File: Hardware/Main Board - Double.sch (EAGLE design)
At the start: 80 parts, among them J1 MICROMOD-2222-C, J10 MICRO-SD-PUSH-PUSH-EXT-PIN, J2 Vertical Qwiic Connector, J4 QWIIC_RIGHT_ANGLE, J5 CORTEX_JTAG_DEBUG_MINIMUM_PTH, J6 MICROMOD_FUNCTION_MAIN, J7 MICROMOD_FUNCTION_MAIN, Q1 3.1A/30V/105mΩ, U1 STG3856QTR, U2 MCP73831, U3 ESD Diode, U4 3.3V, U5 AP7361C-33

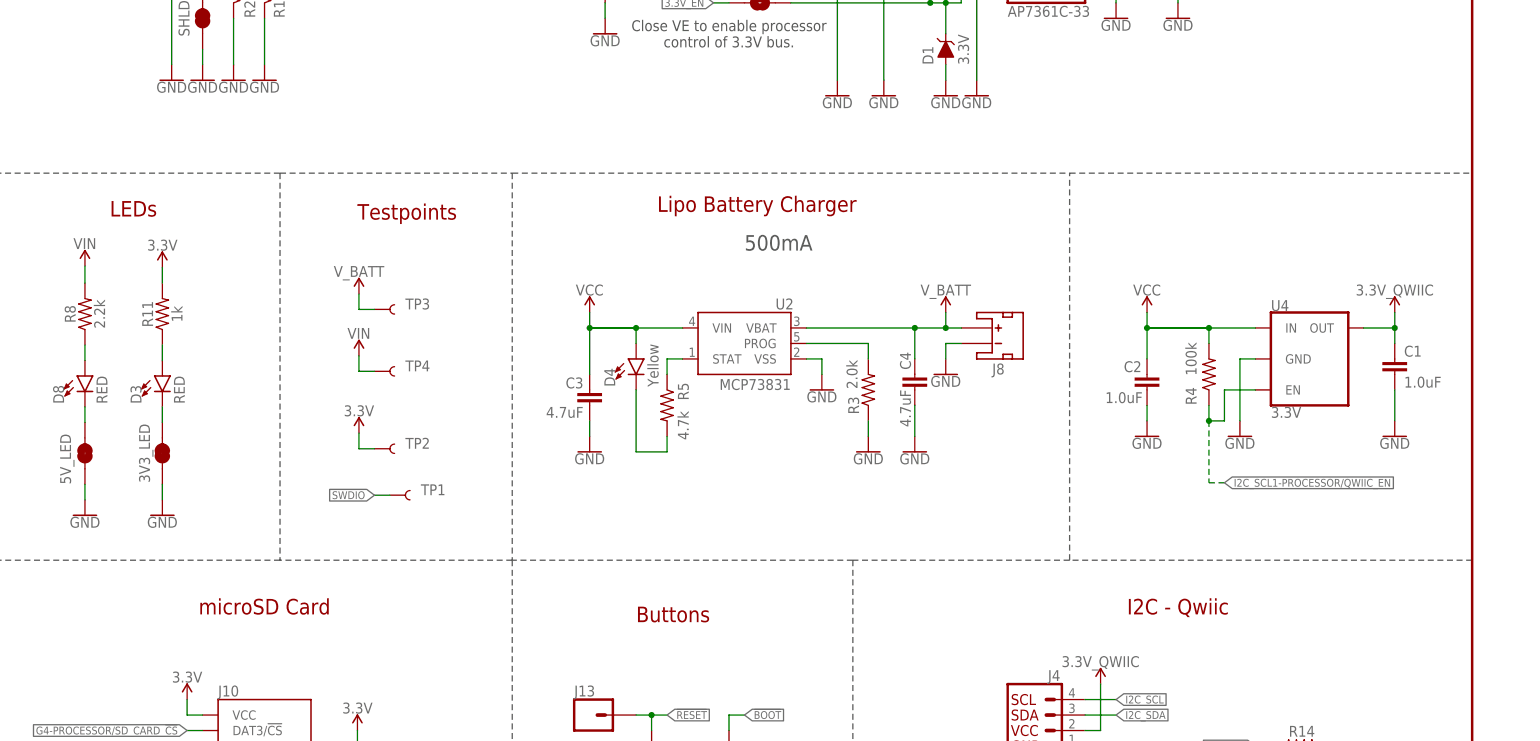
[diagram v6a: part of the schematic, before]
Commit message: Updates text in schematic
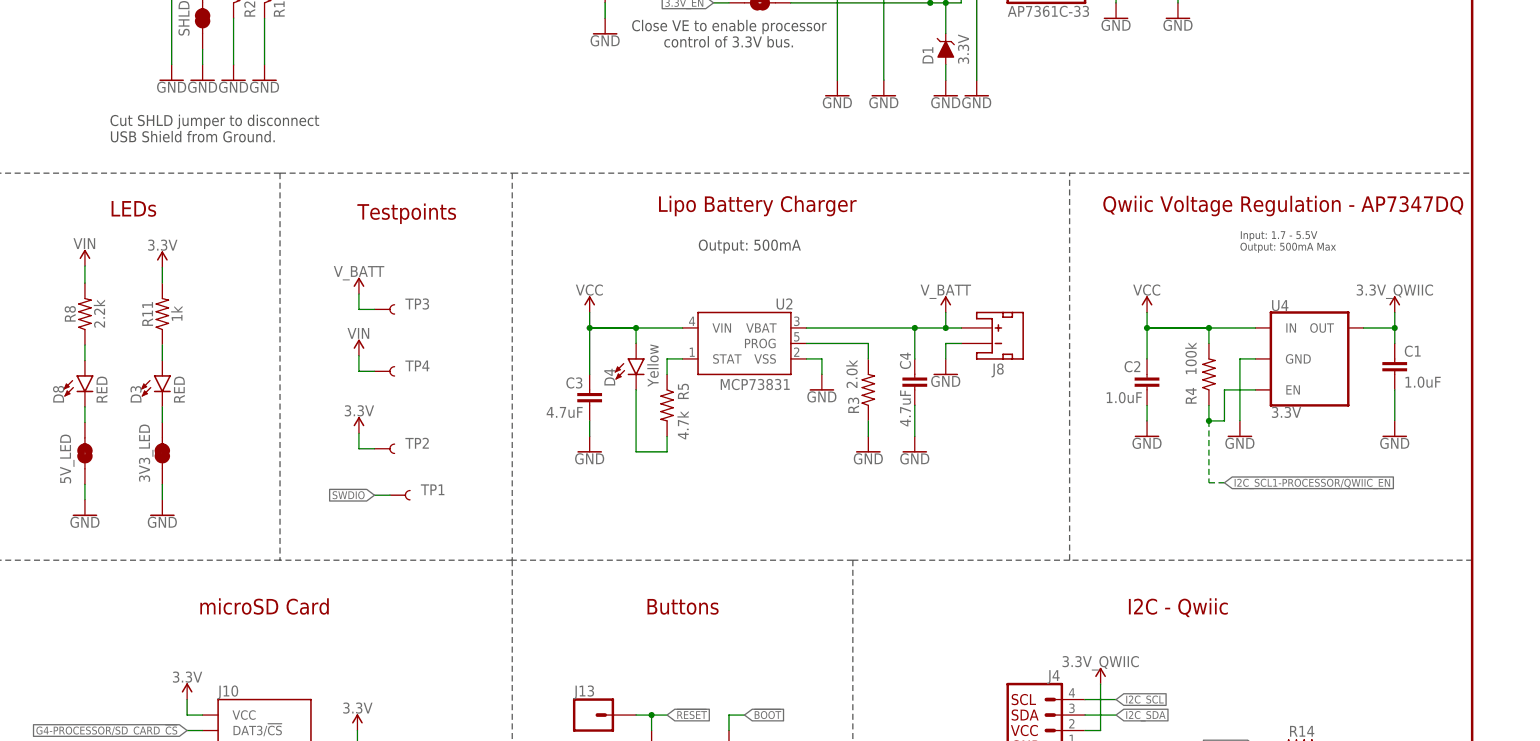
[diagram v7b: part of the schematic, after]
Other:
- note added: "Cut SHLD jumper to disconnect USB Shield from Ground."
- note added: "Input: 1.7 - 5.5V Output: 500mA Max"
- note added: "Output: 500mA"
- note added: "Qwiic Voltage Regulation - AP7347DQ"
- note removed: "500mA"
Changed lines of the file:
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@@
 <wire x1="274.32" y1="76.2" x2="330.2" y2="76.2" width="0.2032" layer="97" style="longdash"/>
 <wire x1="274.32" y1="195.58" x2="274.32" y2="132.08" width="0.2032" layer="97" style="longdash"/>
-<text x="294.64" y="121.92" size="2.54" layer="94" font="vector">Buttons</text>
+<text x="302.26" y="124.46" size="2.54" layer="94" font="vector" align="center">Buttons</text>
 <text x="350.52" y="10.16" size="2.54" layer="94" font="vector">Elias Santistevan</text>
-<text x="323.596" y="185.42" size="2.54" layer="97" font="vector" rot="R180">500mA</text>
 <wire x1="165.1" y1="0" x2="165.1" y2="27.94" width="0.2032" layer="97" style="longdash"/>
 <wire x1="165.1" y1="27.94" x2="187.96" y2="27.94" width="0.2032" layer="97" style="longdash"/>
@@
 <text x="259.08" y="68.58" size="2.54" layer="94" font="vector" align="center">UART Multiplexer</text>
 <wire x1="365.76" y1="132.08" x2="365.76" y2="195.58" width="0.2032" layer="97" style="longdash"/>
+<text x="400.812" y="190.5" size="2.54" layer="94" font="vector" align="center">Qwiic Voltage Regulation - AP7347DQ</text>
+<text x="393.7" y="182.88" size="1.27" layer="97" font="vector">Input: 1.7 - 5.5V
+Output: 500mA Max</text>
+<text x="304.8" y="182.88" size="1.778" layer="97" font="vector">Output: 500mA </text>
+<text x="208.28" y="200.66" size="1.778" layer="97" font="vector">Cut SHLD jumper to disconnect
+USB Shield from Ground. </text>
 </plain>
 <instances>

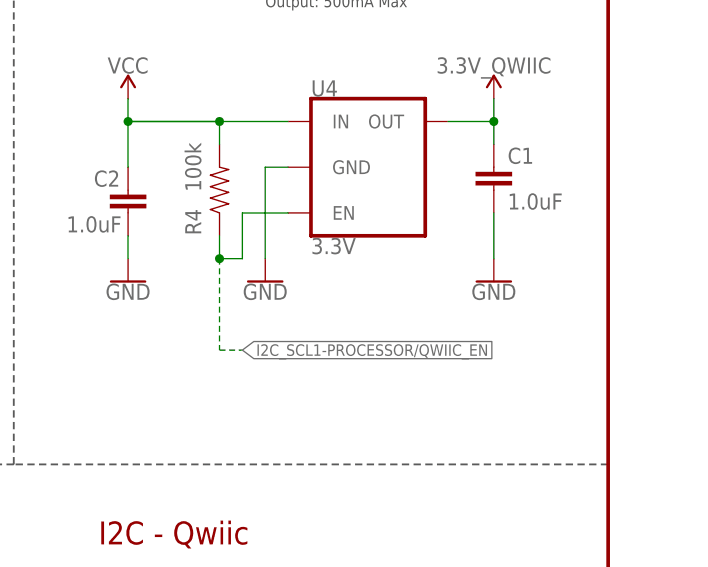
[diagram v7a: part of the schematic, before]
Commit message: Updates device name and removes value from new VREG
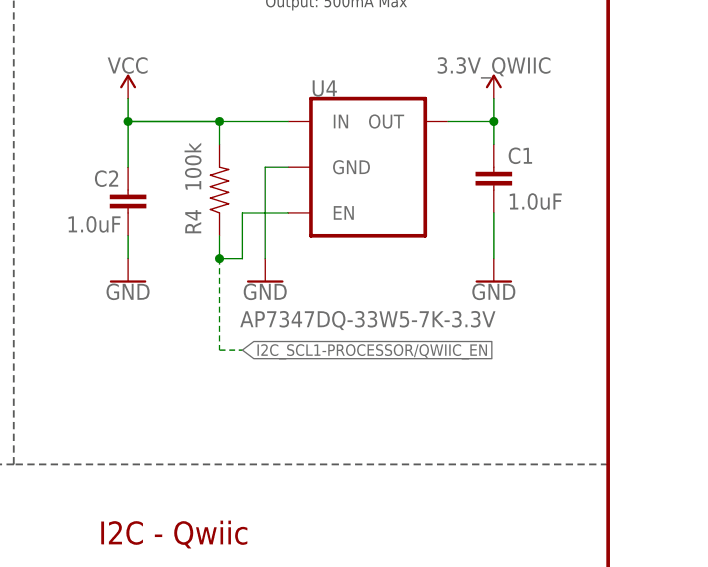
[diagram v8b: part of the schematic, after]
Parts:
- U4: value 3.3V -> AP7347DQ-33W5-7K-3.3V; device dip_switch:V_REG_AP7347DQK-3.3V -> dip_switch:AP7347DQ-33W5-7K-3.3V
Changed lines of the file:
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@@
 <part name="GND24" library="SparkFun-PowerSymbols" deviceset="GND" device=""/>
 <part name="SUPPLY31" library="SparkFun-PowerSymbols" deviceset="V_USB" device=""/>
-<part name="U4" library="dip_switch" deviceset="V_REG_AP7347DQ" device="K-3.3V" value="3.3V"/>
+<part name="U4" library="dip_switch" deviceset="AP7347DQ-33W5-7" device="K-3.3V" value="AP7347DQ-33W5-7K-3.3V"/>
 <part name="GND22" library="SparkFun-PowerSymbols" deviceset="GND" device=""/>
 <part name="SUPPLY32" library="SparkFun-PowerSymbols" deviceset="VCC" device=""/>
@@
 <instance part="U4" gate="G$1" x="406.4" y="165.1" smashed="yes">
 <attribute name="NAME" x="398.78" y="172.974" size="1.778" layer="95" font="vector"/>
-<attribute name="VALUE" x="398.78" y="157.226" size="1.778" layer="96" font="vector" align="top-left"/>
+<attribute name="VALUE" x="390.906" y="149.098" size="1.778" layer="96" font="vector" align="top-left"/>
 </instance>
 <instance part="GND22" gate="1" x="393.7" y="152.4" smashed="yes">
